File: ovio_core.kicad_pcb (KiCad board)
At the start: 6 copper layers, 98 x 27.5 mm, 195 parts, among them J101 Conn_01x06, J301 Conn_01x06, J701 USB3_B_Micro, Q501 NTZD3155C, U101 IP4254CZ8-4-TTL, U102 ECP5U_85_CABGA381, U201 TLV62569DRL, U202 TLV62569DRL, U203 TLV62569DRL, U204 TLV62569DRL, U302 W25Q128JVP, U401 MT9V034, U402 MT9V034, U403 KC2016Z50.0000C15XXK, U501 ISM330DHC, U601 MT41J128M16JT-125:K, U701 FT600Q, U702 PUSB3FR4Z, Y701 30 MHz

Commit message: Added comments and fixed ERC erros
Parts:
- U403: value KC2016Z50.0000C15XXK -> 25 MHz
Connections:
- net /2x cameras/50MHZ_PLL_IN renamed /2x cameras & FPGA Clock/CLOCK_PLL_IN
- net /2x cameras/CAM0_D0 renamed /2x cameras & FPGA Clock/CAM0_D0
- net /2x cameras/CAM0_D0_P renamed /2x cameras & FPGA Clock/CAM0_D0_P
- net /2x cameras/CAM0_D1 renamed /2x cameras & FPGA Clock/CAM0_D1
- net /2x cameras/CAM0_D1_P renamed /2x cameras & FPGA Clock/CAM0_D1_P
- net /2x cameras/CAM0_D2 renamed /2x cameras & FPGA Clock/CAM0_D2
- net /2x cameras/CAM0_D2_P renamed /2x cameras & FPGA Clock/CAM0_D2_P
- net /2x cameras/CAM0_D3 renamed /2x cameras & FPGA Clock/CAM0_D3
- net /2x cameras/CAM0_D3_P renamed /2x cameras & FPGA Clock/CAM0_D3_P
- net /2x cameras/CAM0_D4 renamed /2x cameras & FPGA Clock/CAM0_D4
- net /2x cameras/CAM0_D4_P renamed /2x cameras & FPGA Clock/CAM0_D4_P
- net /2x cameras/CAM0_D5 renamed /2x cameras & FPGA Clock/CAM0_D5
- net /2x cameras/CAM0_D5_P renamed /2x cameras & FPGA Clock/CAM0_D5_P
- net /2x cameras/CAM0_D6 renamed /2x cameras & FPGA Clock/CAM0_D6
- net /2x cameras/CAM0_D6_P renamed /2x cameras & FPGA Clock/CAM0_D6_P
- net /2x cameras/CAM0_D7 renamed /2x cameras & FPGA Clock/CAM0_D7
- net /2x cameras/CAM0_D7_P renamed /2x cameras & FPGA Clock/CAM0_D7_P
- net /2x cameras/CAM0_D8 renamed /2x cameras & FPGA Clock/CAM0_D8
- net /2x cameras/CAM0_D8_P renamed /2x cameras & FPGA Clock/CAM0_D8_P
- net /2x cameras/CAM0_D9 renamed /2x cameras & FPGA Clock/CAM0_D9
- net /2x cameras/CAM0_D9_P renamed /2x cameras & FPGA Clock/CAM0_D9_P
- net /2x cameras/CAM0_FLASH renamed /2x cameras & FPGA Clock/CAM0_FLASH
- net /2x cameras/CAM0_FLASH_P renamed /2x cameras & FPGA Clock/CAM0_FLASH_P
- net /2x cameras/CAM0_FV renamed /2x cameras & FPGA Clock/CAM0_FV
- net /2x cameras/CAM0_FV_P renamed /2x cameras & FPGA Clock/CAM0_FV_P
- net /2x cameras/CAM0_LV renamed /2x cameras & FPGA Clock/CAM0_LV
- net /2x cameras/CAM0_LV_P renamed /2x cameras & FPGA Clock/CAM0_LV_P
- net /2x cameras/CAM0_PIXCLK renamed /2x cameras & FPGA Clock/CAM0_PIXCLK
- net /2x cameras/CAM0_PIXCLK_P renamed /2x cameras & FPGA Clock/CAM0_PIXCLK_P
- net /2x cameras/CAM0_RESET renamed /2x cameras & FPGA Clock/CAM0_RESET
- net /2x cameras/CAM0_SCLK renamed /2x cameras & FPGA Clock/CAM0_SCLK
- net /2x cameras/CAM0_SDATA renamed /2x cameras & FPGA Clock/CAM0_SDATA
- net /2x cameras/CAM0_SYSCLK renamed /2x cameras & FPGA Clock/CAM0_SYSCLK
- net /2x cameras/CAM0_TRIGGER renamed /2x cameras & FPGA Clock/CAM0_TRIGGER
- net /2x cameras/CAM0_VAA renamed /2x cameras & FPGA Clock/CAM0_VAA
- net /2x cameras/CAM1_D0 renamed /2x cameras & FPGA Clock/CAM1_D0
- net /2x cameras/CAM1_D0_P renamed /2x cameras & FPGA Clock/CAM1_D0_P
- net /2x cameras/CAM1_D1 renamed /2x cameras & FPGA Clock/CAM1_D1
- net /2x cameras/CAM1_D1_P renamed /2x cameras & FPGA Clock/CAM1_D1_P
- net /2x cameras/CAM1_D2 renamed /2x cameras & FPGA Clock/CAM1_D2
- net /2x cameras/CAM1_D2_P renamed /2x cameras & FPGA Clock/CAM1_D2_P
- net /2x cameras/CAM1_D3 renamed /2x cameras & FPGA Clock/CAM1_D3
- net /2x cameras/CAM1_D3_P renamed /2x cameras & FPGA Clock/CAM1_D3_P
- net /2x cameras/CAM1_D4 renamed /2x cameras & FPGA Clock/CAM1_D4
- net /2x cameras/CAM1_D4_P renamed /2x cameras & FPGA Clock/CAM1_D4_P
- net /2x cameras/CAM1_D5 renamed /2x cameras & FPGA Clock/CAM1_D5
- net /2x cameras/CAM1_D5_P renamed /2x cameras & FPGA Clock/CAM1_D5_P
- net /2x cameras/CAM1_D6 renamed /2x cameras & FPGA Clock/CAM1_D6
- net /2x cameras/CAM1_D6_P renamed /2x cameras & FPGA Clock/CAM1_D6_P
- net /2x cameras/CAM1_D7 renamed /2x cameras & FPGA Clock/CAM1_D7
- net /2x cameras/CAM1_D7_P renamed /2x cameras & FPGA Clock/CAM1_D7_P
- net /2x cameras/CAM1_D8 renamed /2x cameras & FPGA Clock/CAM1_D8
- net /2x cameras/CAM1_D8_P renamed /2x cameras & FPGA Clock/CAM1_D8_P
- net /2x cameras/CAM1_D9 renamed /2x cameras & FPGA Clock/CAM1_D9
- net /2x cameras/CAM1_D9_P renamed /2x cameras & FPGA Clock/CAM1_D9_P
- net /2x cameras/CAM1_FLASH renamed /2x cameras & FPGA Clock/CAM1_FLASH
- net /2x cameras/CAM1_FLASH_P renamed /2x cameras & FPGA Clock/CAM1_FLASH_P
- net /2x cameras/CAM1_FV renamed /2x cameras & FPGA Clock/CAM1_FV
- net /2x cameras/CAM1_FV_P renamed /2x cameras & FPGA Clock/CAM1_FV_P
- net /2x cameras/CAM1_LV renamed /2x cameras & FPGA Clock/CAM1_LV
- net /2x cameras/CAM1_LV_P renamed /2x cameras & FPGA Clock/CAM1_LV_P
- net /2x cameras/CAM1_PIXCLK renamed /2x cameras & FPGA Clock/CAM1_PIXCLK
- net /2x cameras/CAM1_PIXCLK_P renamed /2x cameras & FPGA Clock/CAM1_PIXCLK_P
- net /2x cameras/CAM1_RESET renamed /2x cameras & FPGA Clock/CAM1_RESET
- net /2x cameras/CAM1_SCLK renamed /2x cameras & FPGA Clock/CAM1_SCLK
- net /2x cameras/CAM1_SDATA renamed /2x cameras & FPGA Clock/CAM1_SDATA
- net /2x cameras/CAM1_SYSCLK renamed /2x cameras & FPGA Clock/CAM1_SYSCLK
- net /2x cameras/CAM1_TRIGGER renamed /2x cameras & FPGA Clock/CAM1_TRIGGER
- net /2x cameras/CAM1_VAA renamed /2x cameras & FPGA Clock/CAM1_VAA
- net /USB Interface/D_N renamed /USB FIFO Interface/D_N
- net /USB Interface/D_P renamed /USB FIFO Interface/D_P
- net /USB Interface/FT_BE0 renamed /USB FIFO Interface/FT_BE0
- net /USB Interface/FT_BE1 renamed /USB FIFO Interface/FT_BE1
- net /USB Interface/FT_CLKOUT renamed /USB FIFO Interface/FT_CLKOUT
- net /USB Interface/FT_D0 renamed /USB FIFO Interface/FT_D0
- net /USB Interface/FT_D1 renamed /USB FIFO Interface/FT_D1
- net /USB Interface/FT_D10 renamed /USB FIFO Interface/FT_D10
- net /USB Interface/FT_D11 renamed /USB FIFO Interface/FT_D11
- net /USB Interface/FT_D12 renamed /USB FIFO Interface/FT_D12
- net /USB Interface/FT_D13 renamed /USB FIFO Interface/FT_D13
- net /USB Interface/FT_D14 renamed /USB FIFO Interface/FT_D14
- net /USB Interface/FT_D15 renamed /USB FIFO Interface/FT_D15
- net /USB Interface/FT_D2 renamed /USB FIFO Interface/FT_D2
- net /USB Interface/FT_D3 renamed /USB FIFO Interface/FT_D3
- net /USB Interface/FT_D4 renamed /USB FIFO Interface/FT_D4
- net /USB Interface/FT_D5 renamed /USB FIFO Interface/FT_D5
- net /USB Interface/FT_D6 renamed /USB FIFO Interface/FT_D6
- net /USB Interface/FT_D7 renamed /USB FIFO Interface/FT_D7
- net /USB Interface/FT_D8 renamed /USB FIFO Interface/FT_D8
- net /USB Interface/FT_D9 renamed /USB FIFO Interface/FT_D9
- net /USB Interface/FT_GPIO0 renamed /USB FIFO Interface/FT_GPIO0
- net /USB Interface/FT_GPIO1 renamed /USB FIFO Interface/FT_GPIO1
- net /USB Interface/FT_REF renamed /USB FIFO Interface/FT_REF
- net /USB Interface/FT_WAKEUP renamed /USB FIFO Interface/FT_WAKEUP
- net /USB Interface/RX_N renamed /USB FIFO Interface/RX_N
- net /USB Interface/RX_P renamed /USB FIFO Interface/RX_P
- net /USB Interface/TX_N renamed /USB FIFO Interface/TX_N
- net /USB Interface/TX_P renamed /USB FIFO Interface/TX_P
- net /USB Interface/TX_P_N renamed /USB FIFO Interface/TX_P_N
- net /USB Interface/TX_P_P renamed /USB FIFO Interface/TX_P_P
- net /USB Interface/VBUS_IN renamed /USB FIFO Interface/VBUS_IN
- net /USB Interface/~FT_OE renamed /USB FIFO Interface/~FT_OE
- net /USB Interface/~FT_RD renamed /USB FIFO Interface/~FT_RD
- net /USB Interface/~FT_RESET renamed /USB FIFO Interface/~FT_RESET
- net /USB Interface/~FT_RXF renamed /USB FIFO Interface/~FT_RXF
- net /USB Interface/~FT_SIWU renamed /USB FIFO Interface/~FT_SIWU
- net /USB Interface/~FT_TXE renamed /USB FIFO Interface/~FT_TXE
- net /USB Interface/~FT_WR renamed /USB FIFO Interface/~FT_WR
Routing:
- net GND: track 350.1 -> 350.3 mm, vias 169 -> 205

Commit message: Added info to sheets, added hardware version to board
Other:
- board text added: "Hardware version: 1.0"

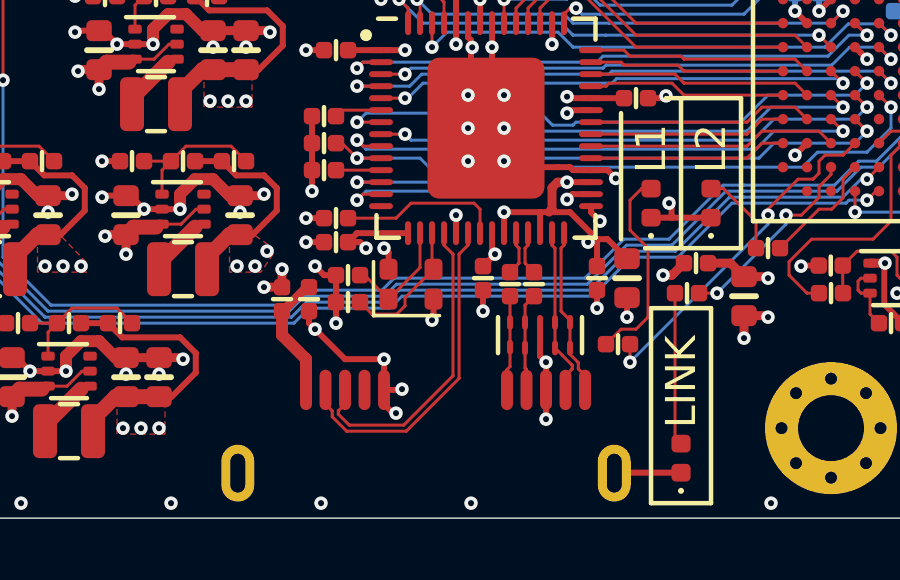
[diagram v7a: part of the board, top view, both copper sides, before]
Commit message: Minor skew fix on HS USB lines
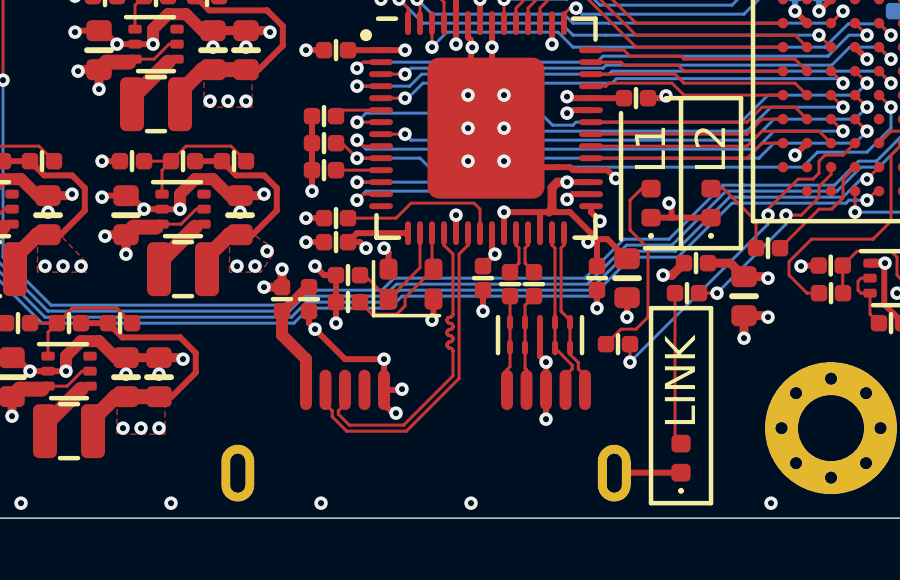
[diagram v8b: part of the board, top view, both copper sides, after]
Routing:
- net /USB FIFO Interface/D_P: track 10.4 -> 11.1 mm
